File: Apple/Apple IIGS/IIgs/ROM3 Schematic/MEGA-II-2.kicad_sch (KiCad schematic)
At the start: 81 parts

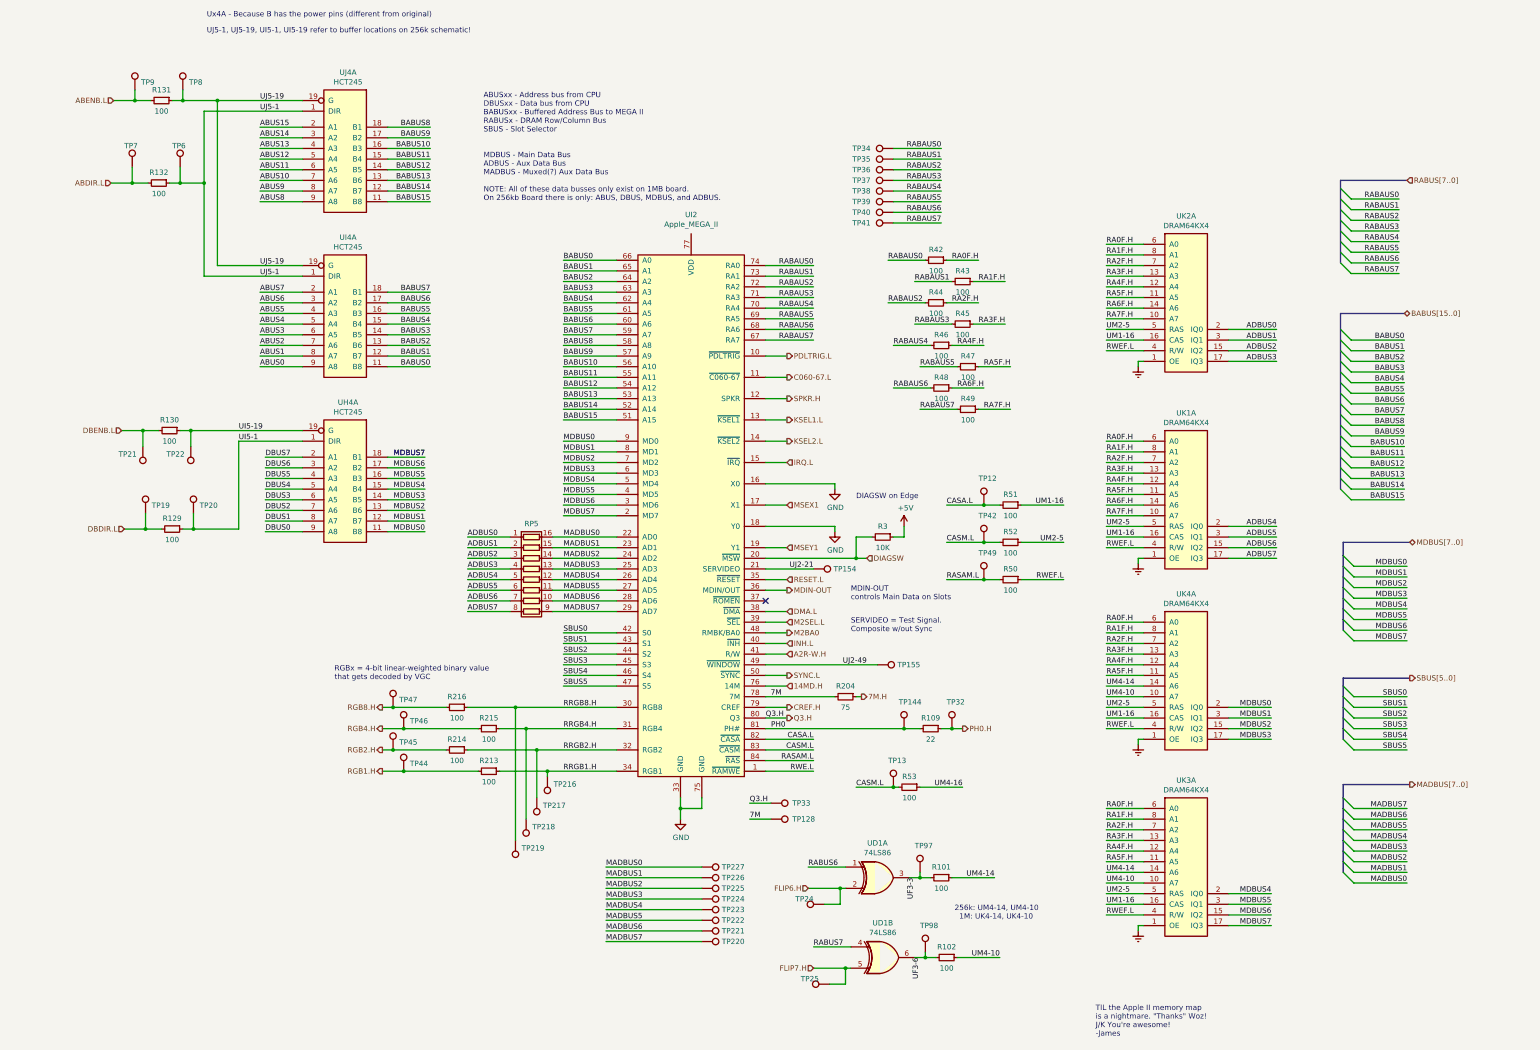
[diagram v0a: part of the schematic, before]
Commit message: 399 ERC, Rescue symbol clean-up
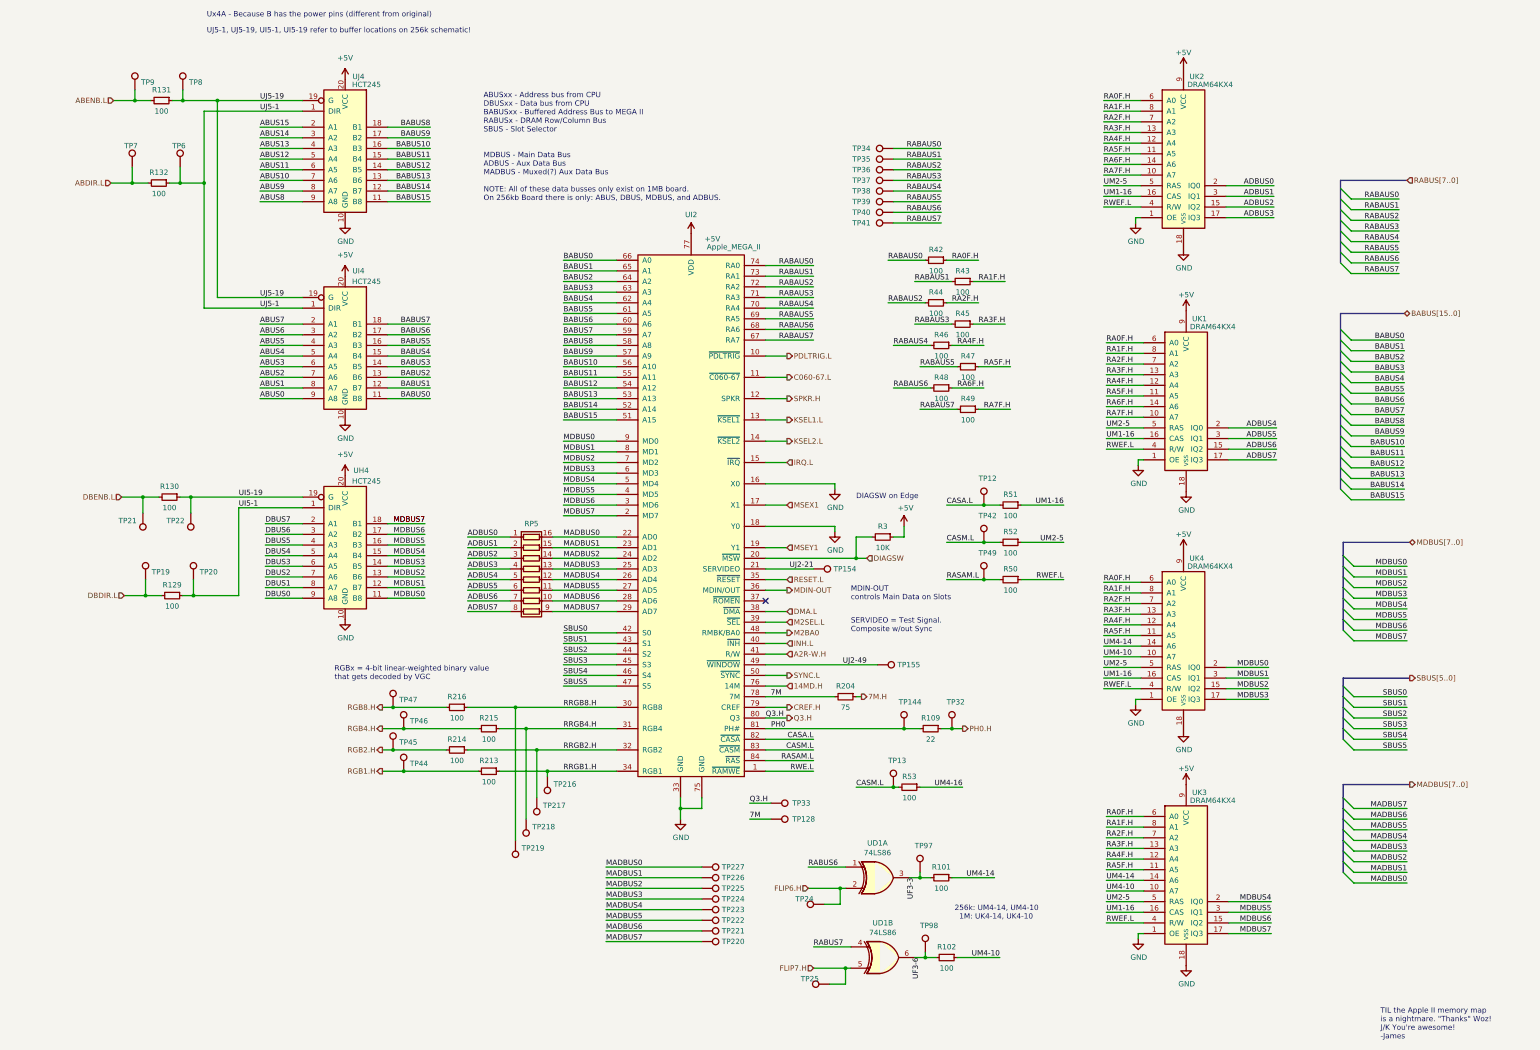
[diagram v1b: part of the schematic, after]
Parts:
- UH4, UI4, UJ4: symbol IIgs-Schematic:HCT245 -> IIgs-Schematic:HCT245-IIgs
- UK1, UK2, UK3, UK4: symbol IIgs-Schematic:DRAM64KX4 -> IIgs-Schematic:DRAM_64KX4
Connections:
- net GNDREF is gone; now on net GND: UK1.1 (OE), UK2.1 (OE), UK3.1 (OE), UK4.1 (OE)
- net +5V: now also UH4.20 (VCC), UI2.77 (VDD), UI4.20 (VCC), UJ4.20 (VCC), UK1.9 (VCC), UK2.9 (VCC), UK3.9 (VCC), UK4.9 (VCC)
- net GND: now also UH4.10 (GND), UI4.10 (GND), UJ4.10 (GND), UK1.18 (VSS), UK2.18 (VSS), UK3.18 (VSS), UK4.18 (VSS)
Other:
- moved on the sheet: R129, R130, TP19, TP20, TP21, TP22

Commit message: 0 ERC Errors AND Warnings. Whew. ICs updated with correct pin assignments and many (many) other fixes.
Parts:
- UD1: value 74LS86 -> F86
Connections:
- net CASM.L: no longer R52.2, TP42.1
- net RABAUS0: no longer UI2.74 (RA0)
- net RABAUS1: no longer UI2.73 (RA1)
- net RABAUS2: no longer UI2.72 (RA2)
- net RABAUS3: no longer UI2.71 (RA3)
- net RABAUS4: no longer UI2.70 (RA4)
- net RABAUS5: no longer UI2.69 (RA5)
- net RABAUS6: no longer UI2.68 (RA6)
- net RABAUS7: no longer UI2.67 (RA7)
- net RABUS6: now also UI2.68 (RA6)
- net RABUS7: now also UI2.67 (RA7)
- net RASAM.L: now also R52.2, TP42.1; no longer R50.2, TP49.1
- net RWE.L: now also R50.2, TP49.1
- net UM1-16: no longer UK3.16 (CAS), UK4.16 (CAS)
- net UM4-16: now also UK3.16 (CAS), UK4.16 (CAS)
- new net RABUS0: UI2.74 (RA0)
- new net RABUS1: UI2.73 (RA1)
- new net RABUS2: UI2.72 (RA2)
- new net RABUS3: UI2.71 (RA3)
- new net RABUS4: UI2.70 (RA4)
- new net RABUS5: UI2.69 (RA5)
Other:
- moved on the sheet: R50, R51, R52, R53, TP12, TP13, TP42, TP49

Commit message: Formatting clean-up
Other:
- note removed: "DIAGSW on Edge"
- note removed: "Ux4A - Because B has the power pins (different from original)"
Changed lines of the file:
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@@
   (title_block
     (title "MEGA-II for IIgs ROM3")
+    (date "2023-01-28")
     (rev "2")
     (company "bald.ee/bitpreserve")
@@
     (effects (font (size 1.27 1.27)) (justify left bottom))
   )
-  (text "Ux4A - Because B has the power pins (different from original)"
-    (at 91.44 20.955 0)
-    (effects (font (size 1.27 1.27)) (justify left bottom))
-  )
-  (text "DIAGSW on Edge" (at 246.38 135.89 0)
-    (effects (font (size 1.27 1.27)) (justify left bottom))
-  )
